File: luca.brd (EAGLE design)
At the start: 65 x 72 mm, 56 parts

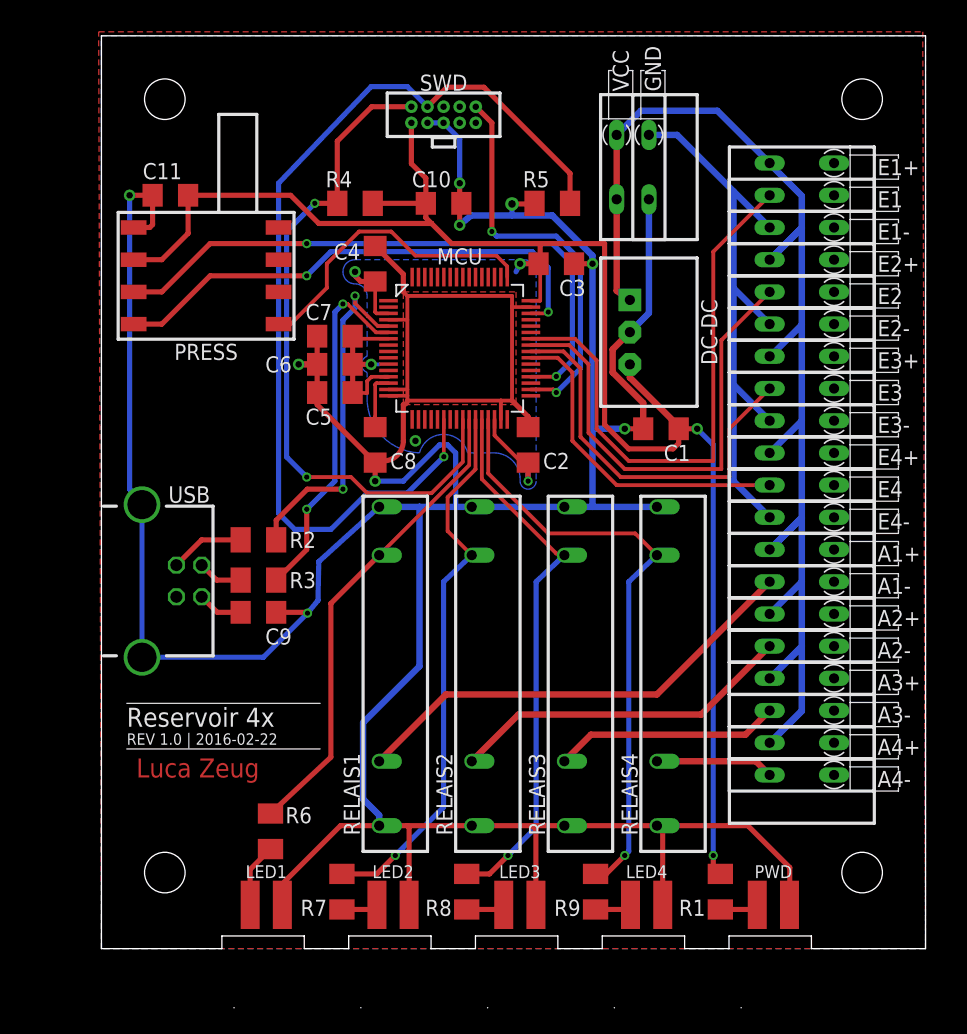
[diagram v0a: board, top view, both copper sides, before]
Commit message: ESD, added Pull-Rs, refactored Dimensions
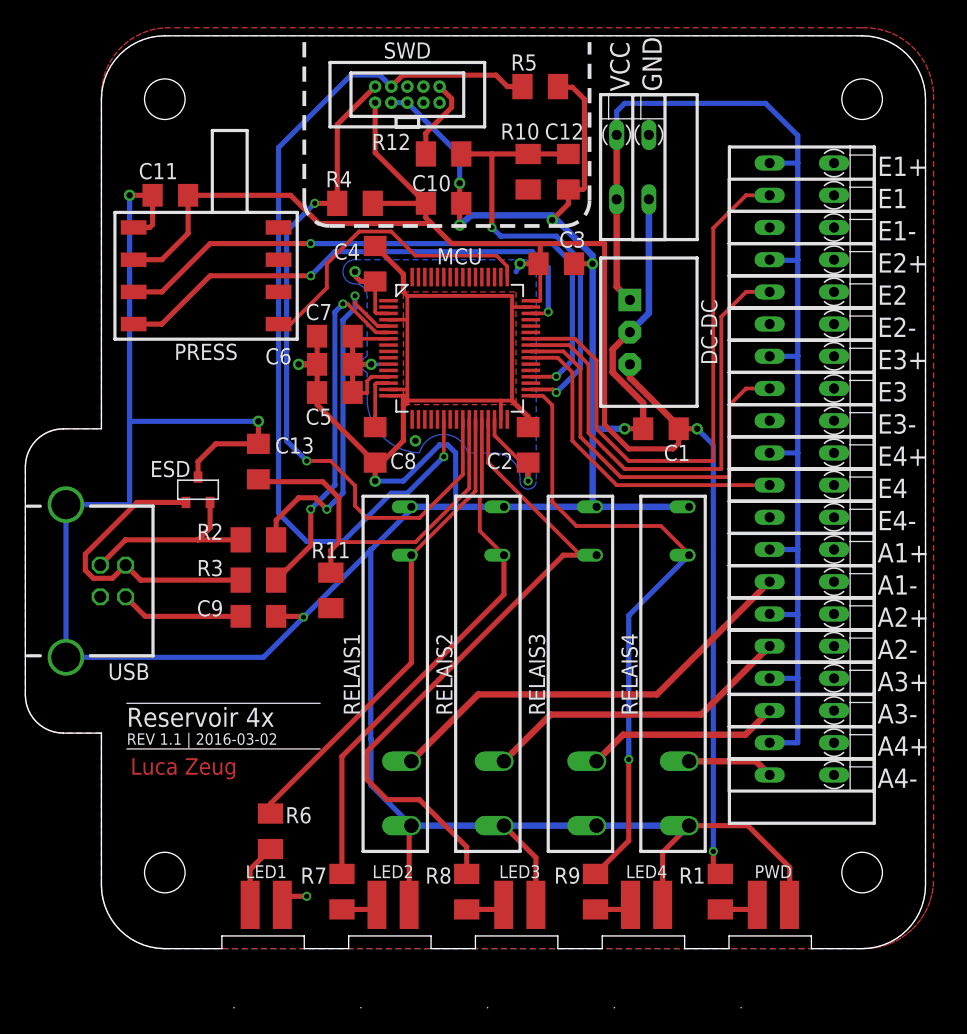
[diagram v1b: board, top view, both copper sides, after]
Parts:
- added C12, C13: 0.1µ, rcl:C1206
- added ESD: GSOT05C-GS08, GSOT05C-GS08:GSOT05C-GS08
- added R10, R11: 10k, rcl:M1206
- added R12: 150, rcl:M1206
- C1: value 10 -> 10µ
- C10, C11, C2, C3, C4, C5, C7, C8: value 0.1 -> 0.1µ
- C6, C9: value 2.2 -> 2.2µ
- moved R5 9.26 mm to (34.6, 68.0), turned to 0 degrees
- moved USB 6.00 mm to (-2.80, 29.0)
- moved SWD 3.27 mm to (24.1, 67.4)
- moved C9 0.32 mm to (12.4, 26.2)
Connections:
- new net N$15: R12.1, SWD.10
- new net NMI_B: C13.1, MCU.26, R11.2
- net A1: now also MCU.27; no longer MCU.26
- net A2: now also MCU.28; no longer MCU.27
- net A3: now also MCU.29; no longer MCU.28
- net A4: now also MCU.33; no longer MCU.29
- net GND: now also C12.2, C13.2, ESD.P$3
- net N$1: now also ESD.P$2
- net N$2: now also ESD.P$1
- net RESET_B: now also C12.1, R10.2, R12.2; no longer SWD.10
- net VDD: now also R10.1, R11.1
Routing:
- net NMI_B: track 0.00 -> 30.6 mm
- net N$2: track 3.56 -> 24.3 mm
- net GND: track 387.7 -> 369.8 mm, vias 9 -> 11
- net VCC: track 112.9 -> 96.7 mm
- net A3: track 43.1 -> 53.5 mm, vias 1 -> 0
- net N$1: track 5.90 -> 15.2 mm
- net N$15: track 0.00 -> 6.55 mm
- net SWD_CLK: track 77.6 -> 71.3 mm
- net N$3: track 3.58 -> 9.71 mm
- net RESET_B: track 31.6 -> 35.7 mm
- net VDD: track 156.6 -> 159.4 mm
- net N$6: track 36.7 -> 34.1 mm
- net N$9: track 17.8 -> 15.3 mm
- net N$14: track 27.3 -> 24.7 mm
- net N$11: track 9.34 -> 6.80 mm
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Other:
- board size 65 x 72 mm -> 71 x 72 mm
- board text added: "REV 1.1 | 2016-03-02"
- board text removed: "REV 1.0 | 2016-02-22"
- board text removed: "Reservoir 4x Kinetis"

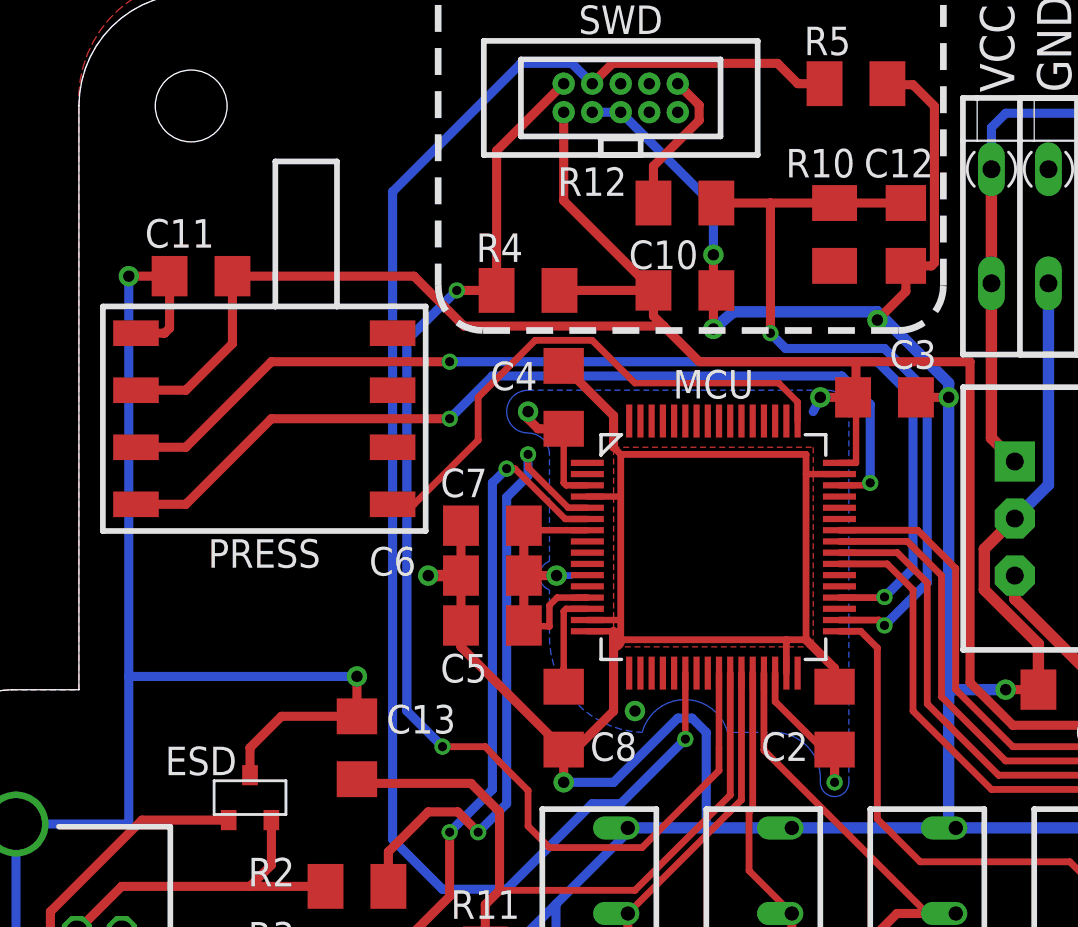
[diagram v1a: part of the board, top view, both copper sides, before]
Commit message: removed unnecessary caps, green LEDs R -> 100
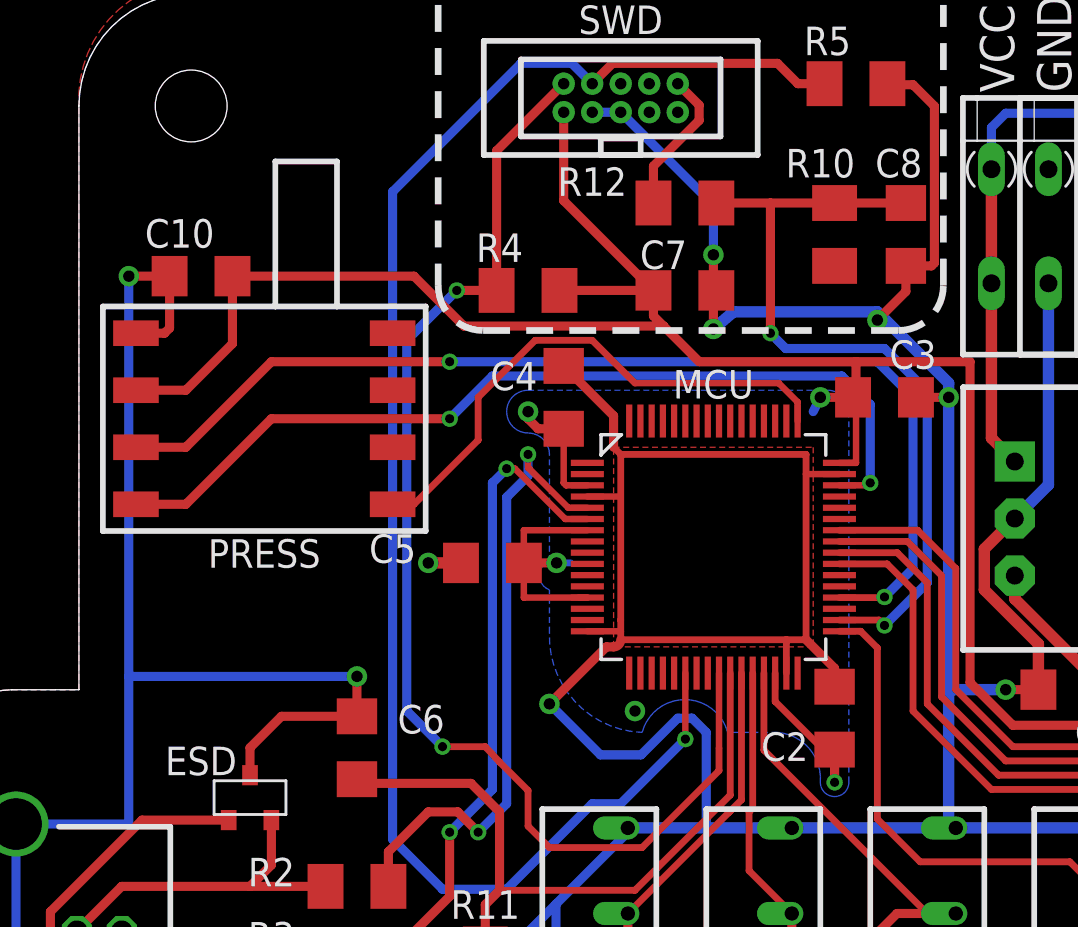
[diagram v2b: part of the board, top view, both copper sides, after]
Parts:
- removed C11, C12, C13: 0.1µ, rcl:C1206
- C5: value 0.1µ -> 2.2µ
- C6: value 2.2µ -> 0.1µ
- R6, R7, R8, R9: value 30 -> 100
- moved C8 26.4 mm to (36.8, 61.3)
- moved C10 21.6 mm to (5.44, 59.4)
- moved C7 13.5 mm to (27.0, 58.8), turned to 0 degrees
- moved C6 9.76 mm to (12.4, 38.4), turned to 90 degrees
- moved C5 2.79 mm to (18.4, 46.6)
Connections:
- removed net AREF: C8.1, MCU.14
- new net VREFL: MCU.15
- new net VREF_/_VREFO: MCU.14
- net GND: now also C10.1; no longer C10.2, C11.1, C12.2, C13.2, MCU.15
- net NMI_B: now also C6.1; no longer C13.1
- net RESET_B: now also C8.1; no longer C12.1
- net VDD: now also C10.2; no longer C10.1, C11.2, C6.1
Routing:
- net GND: track 369.8 -> 352.8 mm
- net AREF: track 4.46 -> 0.00 mm
- net VDD: track 159.4 -> 156.8 mm

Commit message: added config jumper
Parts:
- added J1: (no value), SparkFun-Connectors:1X02_LOCK
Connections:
- new net N$12: J1.1, MCU.20
- new net N$13: J1.2, MCU.21
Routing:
- net N$12: track 0.00 -> 25.1 mm
- net N$13: track 0.00 -> 22.8 mm
- net E1: track 45.4 -> 46.4 mm
- net SWD_DIO: track 55.0 -> 55.9 mm
- net E2: track 38.9 -> 39.5 mm
